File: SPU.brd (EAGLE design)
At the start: 160 x 130 mm, 414 parts, among them Q1 BSS123, Q2 12MHz, Q3 BSS123, Q4 BSS123, Q5 BSS123, Q6 BSS123

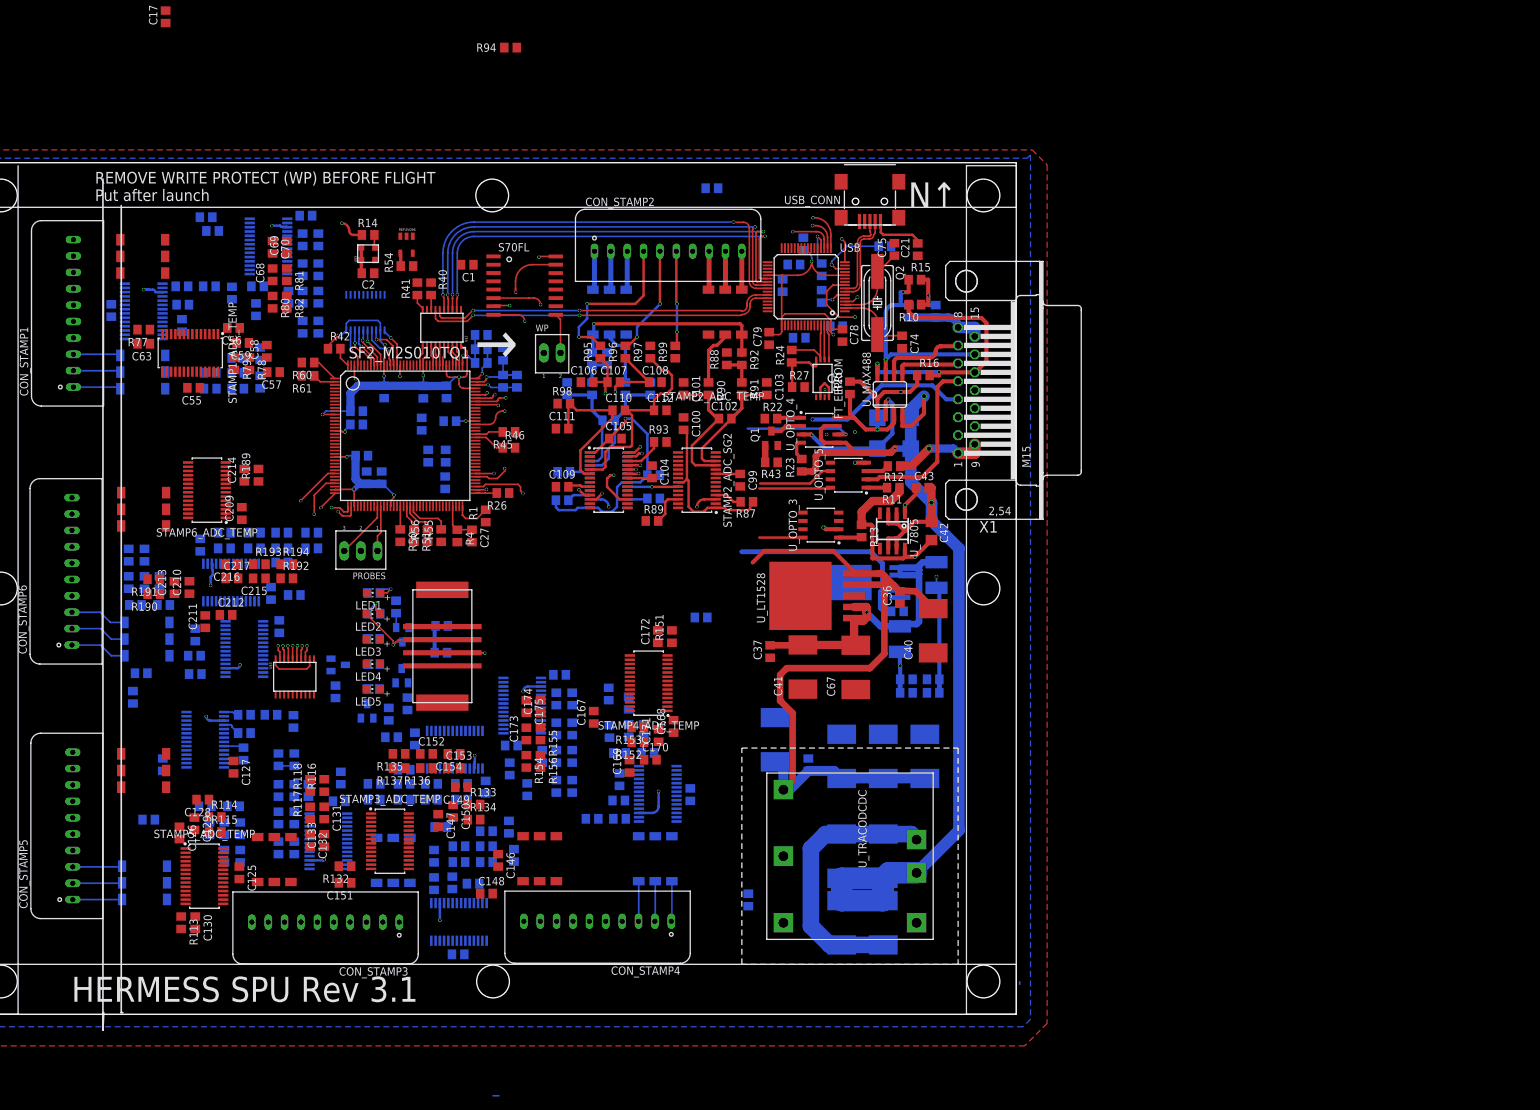
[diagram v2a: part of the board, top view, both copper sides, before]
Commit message: Mid day commit Moved Stamp 3 -5, continue with stamp 6, currently disabled airwires: GND, 3v3 Added names to top and bottom rerouted 4Mhz clk
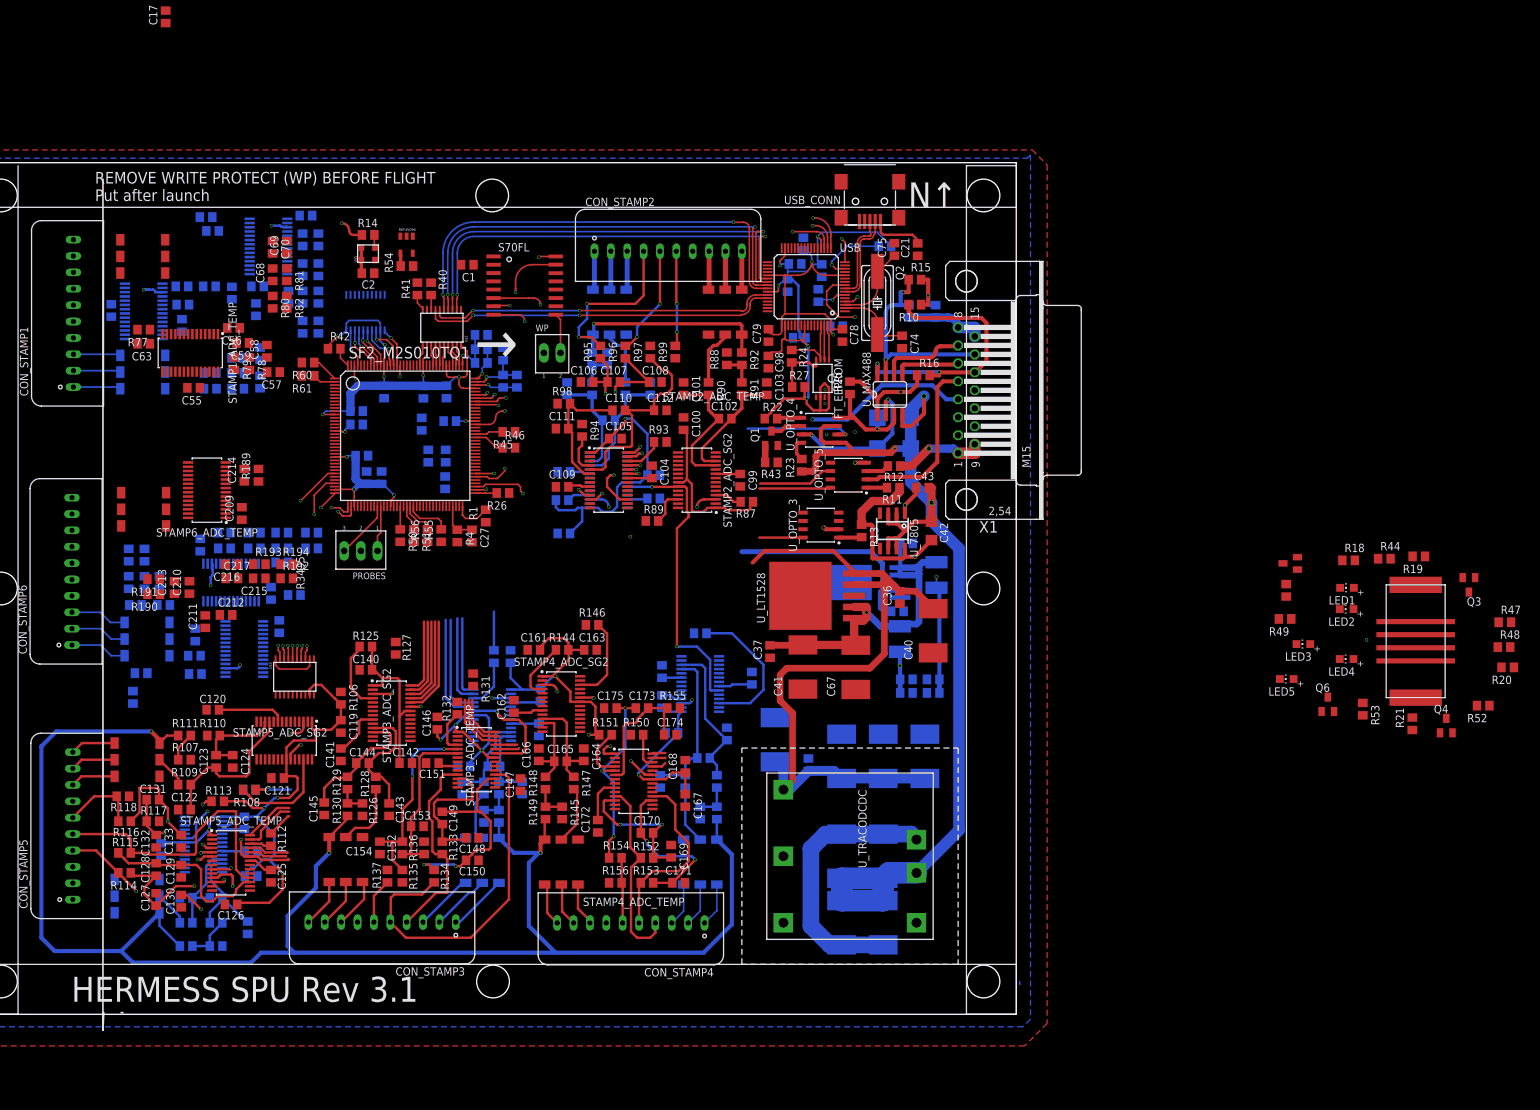
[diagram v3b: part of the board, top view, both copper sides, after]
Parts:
- moved R20 173.1 mm to (235.0, 53.0), flipped to the top
- moved R52 169.5 mm to (231.3, 47.1), flipped to the top
- moved Q3 163.0 mm to (229.1, 65.6), flipped to the top
- moved R48 162.3 mm to (234.5, 56.1), flipped to the top, turned to 0 degrees
- moved R47 162.3 mm to (234.6, 59.8), flipped to the top, turned to 0 degrees
- moved R19 159.8 mm to (221.5, 69.9), flipped to the top, turned to 180 degrees
- moved Q4 159.6 mm to (225.7, 44.1), flipped to the top
- moved R21 153.4 mm to (220.5, 44.3), flipped to the top
- moved R44 151.1 mm to (216.2, 69.5), flipped to the top, turned to 0 degrees
- moved R18 148.9 mm to (210.7, 69.3), flipped to the top, turned to 0 degrees
- moved R53 148.7 mm to (212.9, 46.6), flipped to the top
- moved LED1 148.6 mm to (210.5, 65.1)
- moved LED2 148.6 mm to (210.4, 61.8)
- moved LED4 148.6 mm to (210.4, 54.2)
- moved ZE05H-4P-2V 148.6 mm to (221.0, 56.9)
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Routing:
- net 3V3: track 137.5 -> 463.9 mm, vias 4 -> 19
- net 4V096: track 33.7 -> 285.4 mm, vias 1 -> 4
- net ADC_START: track 12.3 -> 177.5 mm, vias 2 -> 10
- net SG_CLK: track 371.1 -> 287.3 mm, vias 13 -> 14
- net STAMP3_TEMP_AIN2: track 0.00 -> 53.7 mm
- net STAMP5_TEMP_AIN2: track 0.00 -> 43.5 mm
- net STAMP5_TEMP_AIN1: track 0.00 -> 37.2 mm, vias 0 -> 2
- net STAMP3_MOSI: track 0.00 -> 34.2 mm
- net N$150: track 0.00 -> 32.1 mm, vias 0 -> 2
- net STAMP3_SCLK: track 0.00 -> 31.1 mm
- net STAMP3_TEMP_AIN1: track 0.00 -> 30.9 mm
- net N$174: track 0.00 -> 30.2 mm, vias 0 -> 3
- net N$153: track 0.00 -> 29.4 mm, vias 0 -> 2
- net STAMP4_TEMP_AIN1: track 0.00 -> 29.3 mm
- net STAMP4_TEMP_AIN2: track 0.00 -> 28.4 mm
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
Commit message: Routed all signals and voltages End of day commit TODO: GND connection Adding WE - XTAL Eagle lib Update schematic: Adding XTAL Bord: routed
NOTE: DRC not ok
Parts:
- removed LED1, LED2, LED3, LED4, LED5: 1V9, adafruit:CHIP-LED0805
- added C30, C32: 6pF, rcl:C0805
- added FL, MS, MSS, PWR, RC: 1V9, adafruit:CHIP-LED0805
- added RCJ1, RCJ2, Y1J1, Y1J2: (no value), jumper:SJ
- added Y1: 32.768kHz, Eagle_WE-XTAL (rev21c):WE-XTAL_IQXC-90
- moved R52 137.3 mm to (95.8, 69.1), flipped to the bottom
- moved R47 136.1 mm to (98.5, 59.1)
- moved R48 128.2 mm to (106.2, 57.2), turned to 90 degrees
- moved Q3 126.0 mm to (103.4, 57.1), turned to 0 degrees
- moved R19 125.7 mm to (95.8, 66.5), flipped to the bottom
- moved R53 122.3 mm to (92.2, 66.0), turned to 180 degrees
- moved Q6 117.4 mm to (92.3, 69.4)
- moved ZE05H-4P-2V 117.0 mm to (104.3, 65.8), turned to 180 degrees
- moved Q4 115.2 mm to (111.4, 58.8), turned to 90 degrees
- moved R18 115.1 mm to (95.8, 64.0), flipped to the bottom, turned to 180 degrees
- moved R20 114.6 mm to (123.2, 78.0)
- moved R44 113.9 mm to (103.4, 53.8), turned to 180 degrees
- moved R21 106.7 mm to (114.8, 58.9), turned to 270 degrees
- moved R34 98.6 mm to (103.2, 74.7), flipped to the bottom, turned to 270 degrees
- moved Q5 95.2 mm to (106.8, 74.7), flipped to the bottom
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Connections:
- removed net N$33: C27.1, R4.1, SF2_M2S010TQ1.69
- new net AUX_EXTAL: RCJ1.1, SF2_M2S010TQ1.69, Y1J2.2
- new net AUX_XTAL: RCJ2.1, SF2_M2S010TQ1.68, Y1J1.1
- new net N$76: C32.1, Y1.2, Y1J2.1
- new net N$8: C30.1, Y1.1, Y1J1.2
- new net NET_U: C27.1, R4.1, RCJ1.2
- net 3V3: now also RCJ2.2; no longer SF2_M2S010TQ1.68
- net GND: now also C30.2, C32.2, PWR.C; no longer LED1.C
- net N$175: now also RC.A; no longer LED3.A
- net N$177: now also RC.C; no longer LED3.C
- net N$181: now also FL.C; no longer LED2.C
- net N$30: now also PWR.A; no longer LED1.A
- net N$31: now also MS.C; no longer LED5.C
- net N$32: now also MSS.C; no longer LED4.C
- net N$45: now also FL.A; no longer LED2.A
- net N$51: now also MSS.A; no longer LED4.A
- net N$77: now also MS.A; no longer LED5.A
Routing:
- net 3V3: track 463.9 -> 1103.8 mm, vias 19 -> 53
- net 5V: track 116.6 -> 508.0 mm, vias 0 -> 3
- net 4V096: track 285.4 -> 546.2 mm, vias 4 -> 7
- net ADC_START: track 177.5 -> 301.6 mm, vias 10 -> 17
- net 1V2: track 135.6 -> 249.0 mm, vias 10 -> 14
- net STAMP6_SCLK: track 0.00 -> 97.6 mm, vias 0 -> 4
- net WP: track 6.12 -> 100.1 mm, vias 0 -> 1
- net STAMP4_MOSI: track 1.96 -> 93.8 mm, vias 0 -> 6
- net SOE: track 6.67 -> 96.1 mm, vias 0 -> 2
- net LO: track 10.9 -> 98.6 mm, vias 0 -> 3
- net TM_TX: track 2.58 -> 89.7 mm, vias 0 -> 2
- net SODS: track 11.5 -> 96.9 mm, vias 0 -> 4
- net STAMP5_CS_TEMP: track 5.75 -> 91.0 mm, vias 0 -> 3
- net STAMP4_MISO: track 0.00 -> 82.8 mm, vias 0 -> 3
- net STAMP6_MOSI: track 0.00 -> 82.2 mm, vias 0 -> 4
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
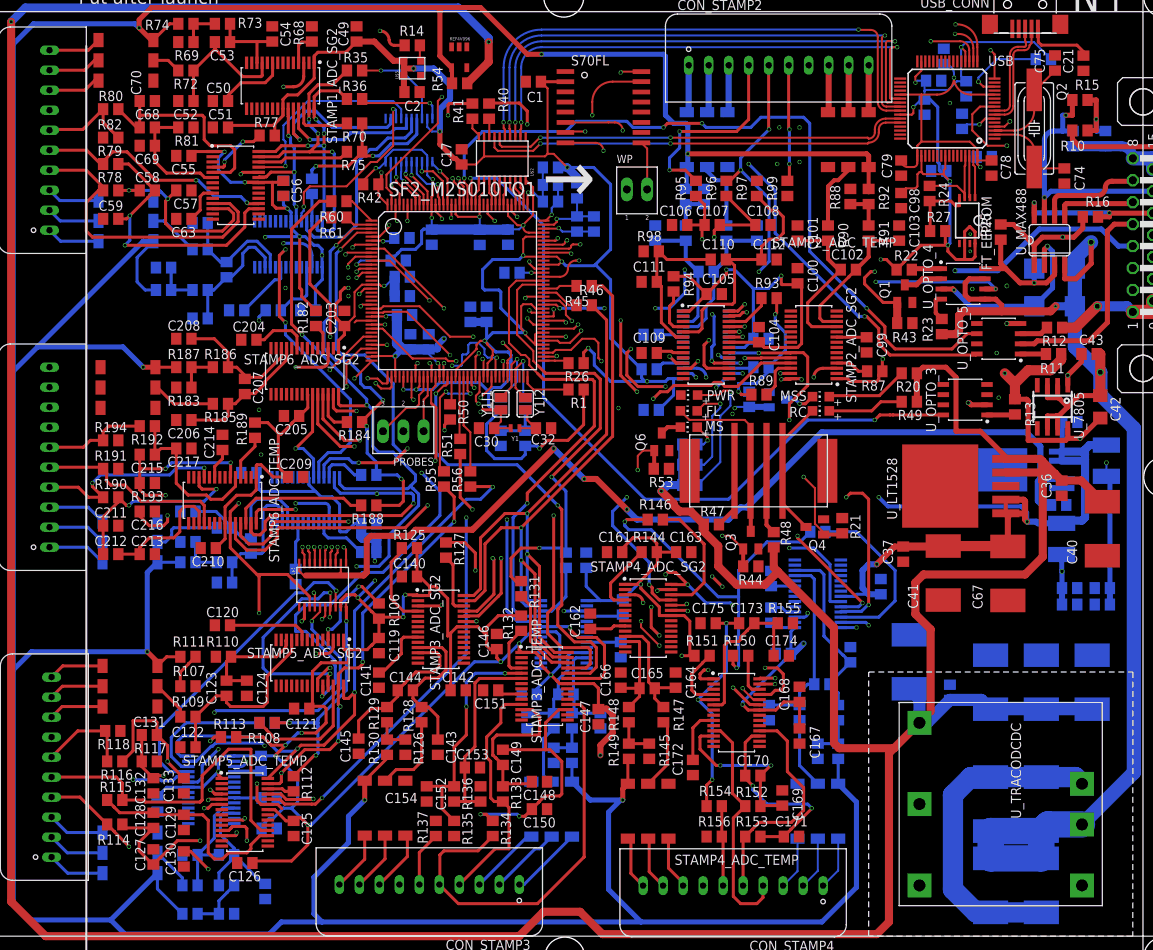
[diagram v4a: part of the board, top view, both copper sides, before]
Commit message: Adding vias 54 airwires
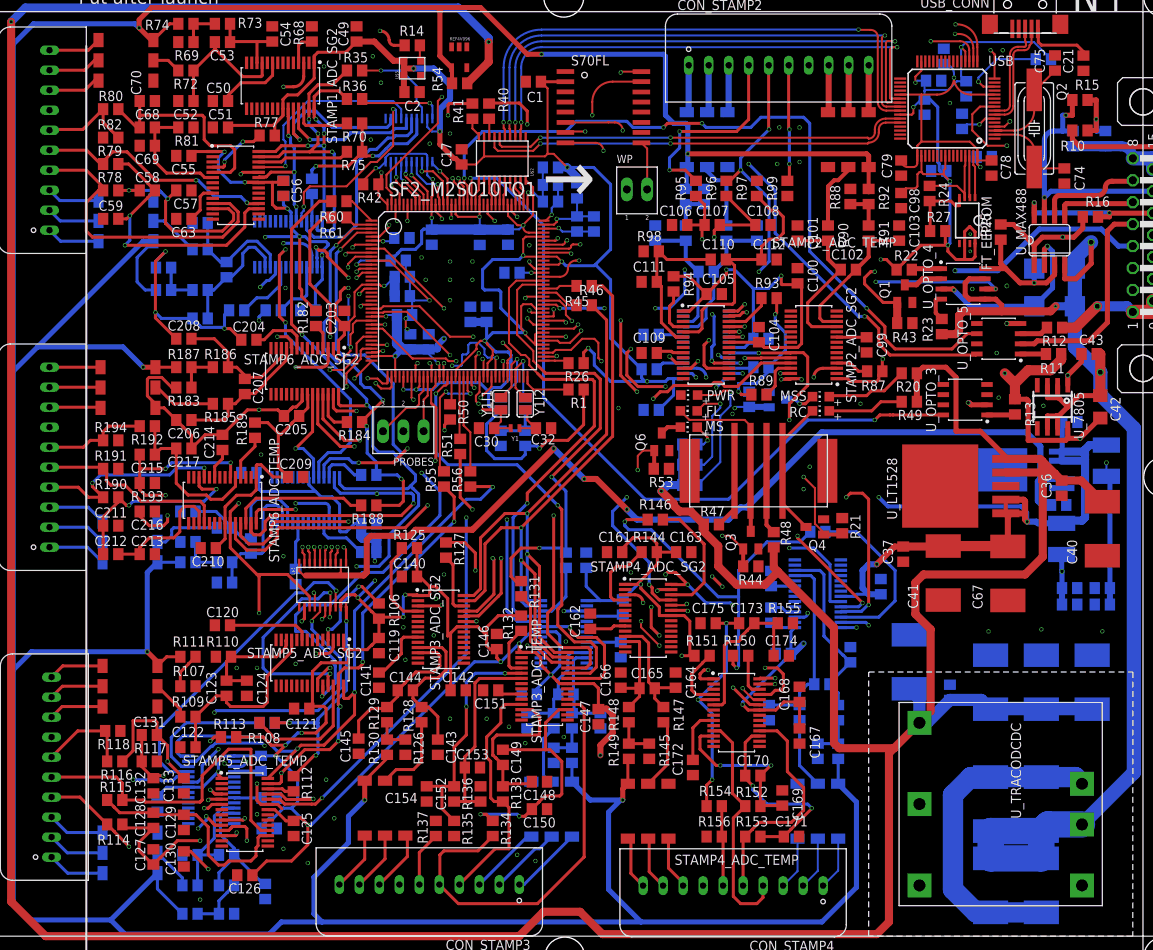
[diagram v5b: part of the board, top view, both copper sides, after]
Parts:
- moved C126 1.52 mm to (40.1, 15.2)
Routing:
- net GND: track 39.4 -> 210.5 mm, vias 29 -> 90
- net STAMP6_SG2_AIN3: track 0.00 -> 6.41 mm
- net STAMP6_SG2_AIN2: track 0.00 -> 6.39 mm
- net STAMP6_SG2_AIN1: track 0.00 -> 6.38 mm
- net STAMP6_CS_SG1: track 46.7 -> 51.0 mm
- net 3V3: track 1103.8 -> 1106.0 mm
- net N$129: track 27.0 -> 28.2 mm
- net N$68: track 32.0 -> 33.0 mm
- net N$161: track 9.18 -> 9.97 mm
